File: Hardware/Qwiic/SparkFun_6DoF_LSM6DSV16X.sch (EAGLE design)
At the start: 31 parts, among them J1 QWIIC_RIGHT_ANGLE, J2 QWIIC_RIGHT_ANGLE, U2 LSM6DSV16X

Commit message: Changes design to design with filter
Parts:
- removed FRAME1: FRAME-LETTER, SparkFun-Aesthetics:FRAME-LETTER
- added C1, C2, C5, C6: 110pF, SparkFun-Capacitors:CAP-0603
- added FRAME2: FRAME-LEDGER, SparkFun-Aesthetics:FRAME-LEDGER
- added R7, R8: 0, SparkFun-Resistors:0OHM-0603-1/10W
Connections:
- removed net SCX: JP3.4, SCX.2, U2.SCX/AH2/QVAR2
- removed net SDX/PICO_AUX: JP3.5, SDX.2, U2.SDX/AH1/QVAR1
- new net SCX/AH2/QVAR2: C5.1, JP3.4, R8.2
- new net SCX/AH2/QVAR2_FILTER: C2.1, R8.1, SCX.2, U2.SCX/AH2/QVAR2
- new net SDX/AH1/QVAR1: C6.1, JP3.5, R7.2
- new net SDX/AH1/QVAR1_FILTER: C1.1, R7.1, SDX.2, U2.SDX/AH1/QVAR1
- net GND: now also C1.2, C2.2, C5.2, C6.2
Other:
- note added: "Cut SCX and SDX jumpers to utilize QVAR lines."
- note added: "DNP"
- note added: "If using Mode 2 (Sensor Hub Mode), or QVAR lines cut both traces."
- note added: "Pass Band FIlter - Electrodes"
- note added: "v01"
- note removed: "If using Mode 2 (Sensor Hub Mode), cut both traces."
- note removed: "v10"
- moved on the sheet: ADDR, C3, C4, D1, I2C_PU, J1, J2, JP1, JP3, LED, R1, R2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

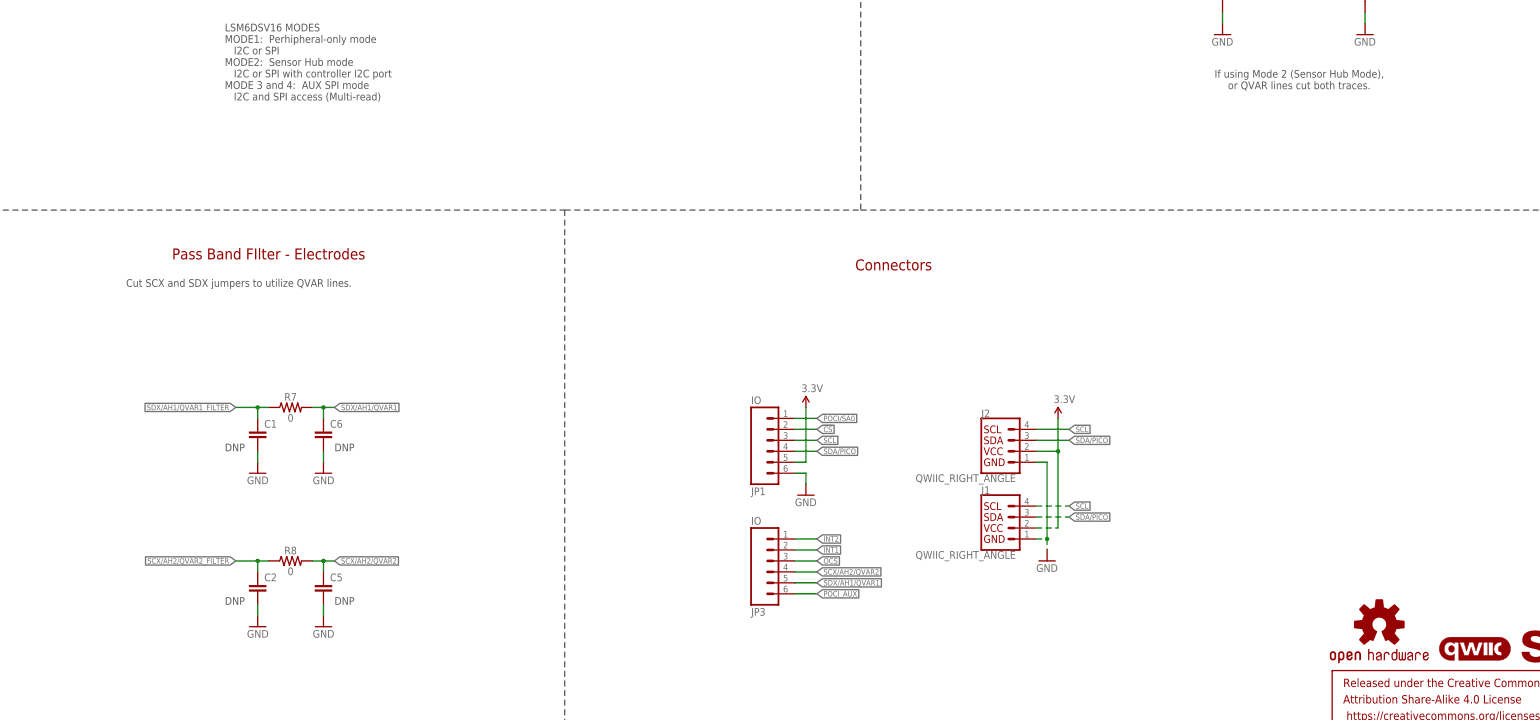
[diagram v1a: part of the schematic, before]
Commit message: Adds labels, fixes various DRC issues
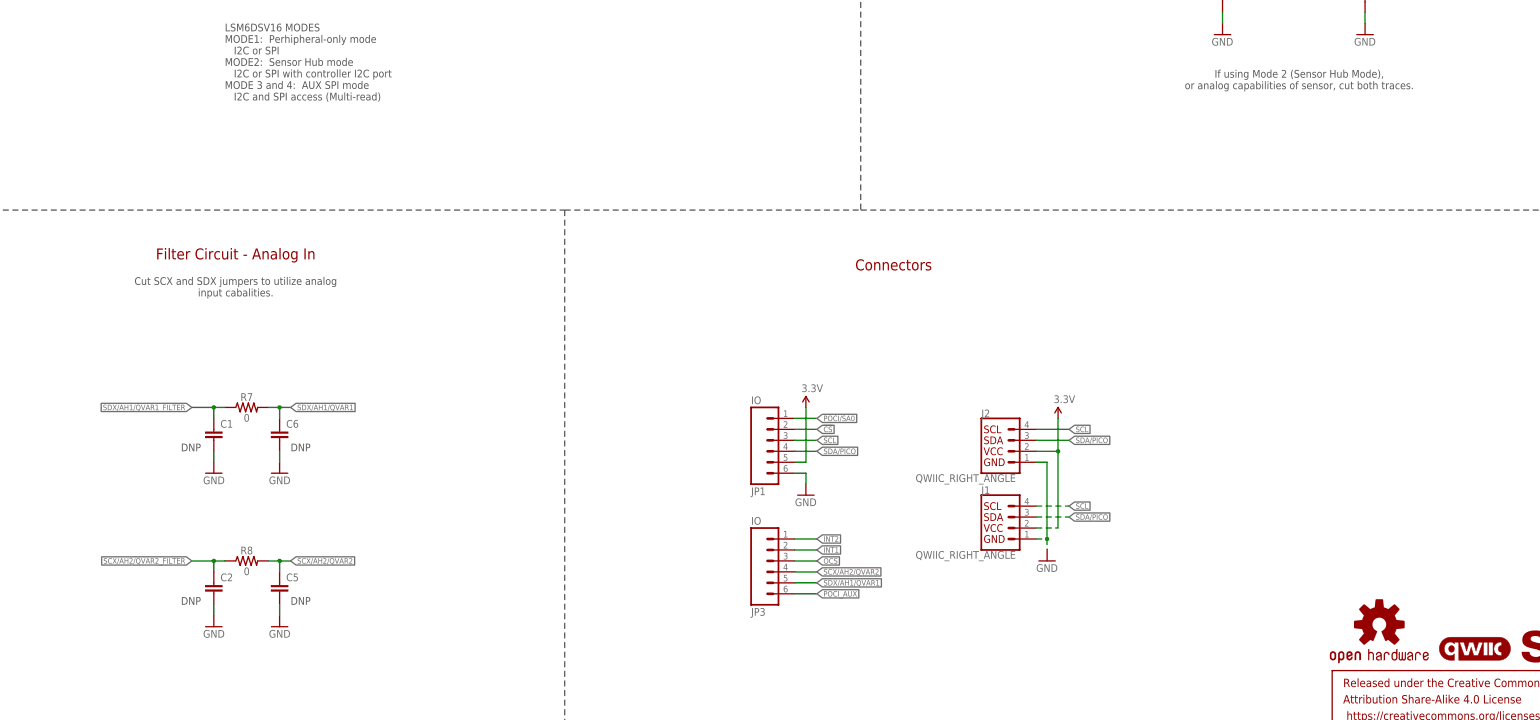
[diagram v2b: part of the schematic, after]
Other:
- note added: "Cut SCX and SDX jumpers to utilize analog input cabalities."
- note added: "Filter Circuit - Analog In"
- note added: "If using Mode 2 (Sensor Hub Mode), or analog capabilities of sensor, cut both traces."
- note removed: "Cut SCX and SDX jumpers to utilize QVAR lines."
- note removed: "If using Mode 2 (Sensor Hub Mode), or QVAR lines cut both traces."
- note removed: "Pass Band FIlter - Electrodes"
- moved on the sheet: C1, C2, C5, C6, R7, R8

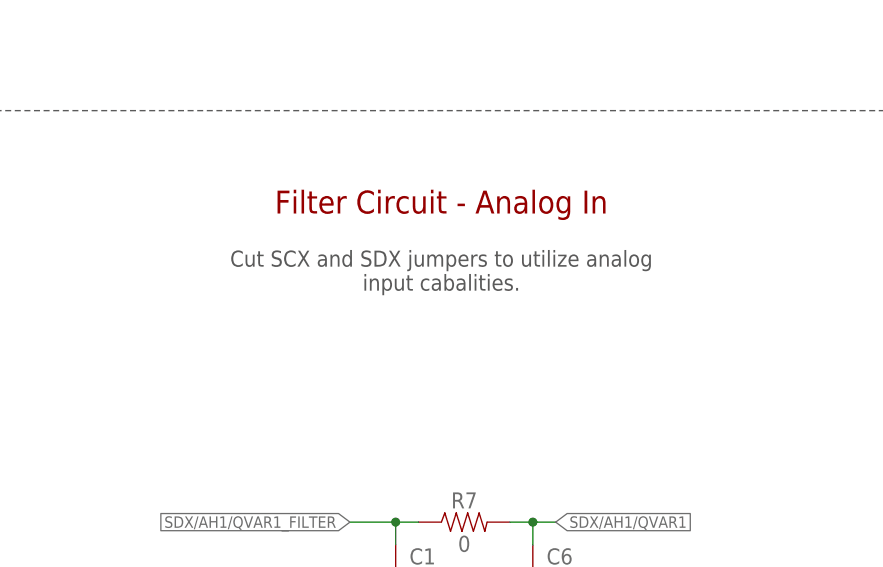
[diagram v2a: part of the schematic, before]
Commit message: Updates part with silk outline
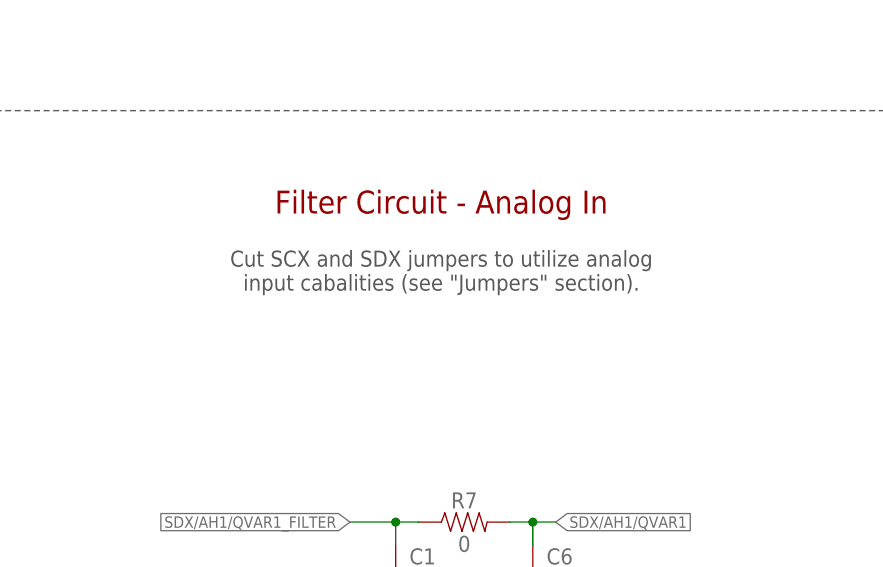
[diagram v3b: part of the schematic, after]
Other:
- note added: "Cut SCX and SDX jumpers to utilize analog input cabalities (see "Jumpers" section)."
- note removed: "Cut SCX and SDX jumpers to utilize analog input cabalities."
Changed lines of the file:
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@@
 <text x="76.2" y="132.08" size="2.54" layer="94" font="vector" align="center">Filter Circuit - Analog In</text>
 <text x="76.2" y="124.46" size="1.778" layer="97" font="vector" align="center">Cut SCX and SDX jumpers to utilize analog
-input cabalities.</text>
+input cabalities (see "Jumpers" section).</text>
 <text x="63.5" y="86.36" size="1.778" layer="97" font="vector">DNP</text>
 <text x="88.9" y="86.36" size="1.778" layer="97" font="vector">DNP</text>
